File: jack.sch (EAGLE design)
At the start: 21 parts, among them IC1 NUF2221W1T2G, IC2 ATSAMD21G18, IC3 LDO, SW1 SPST

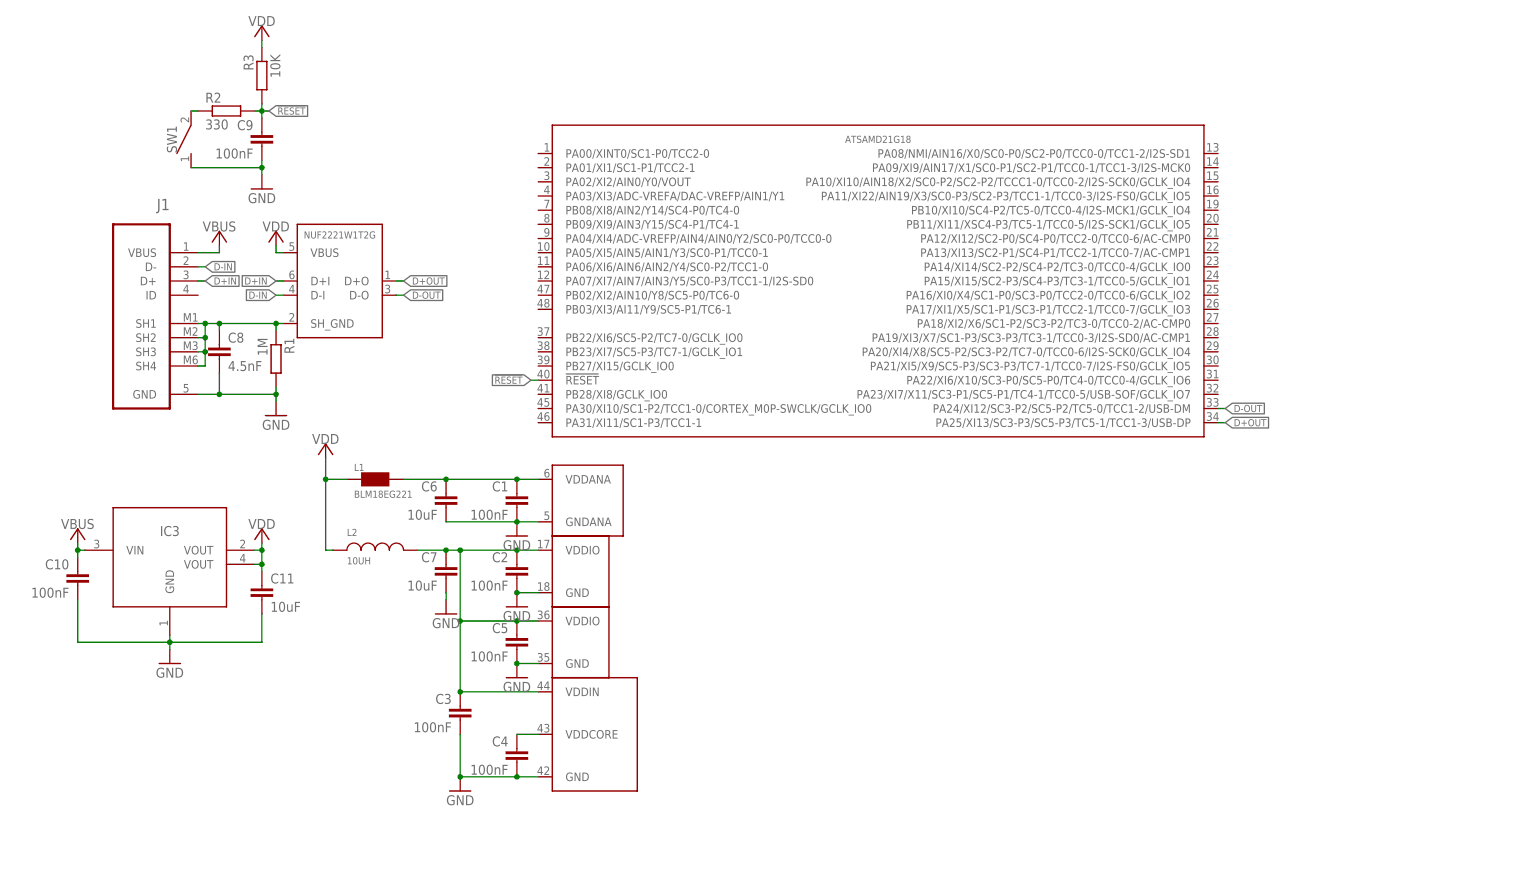
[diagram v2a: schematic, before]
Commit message: :goat: Added 24 MHZ crystal
Added 24 MHZ crystal
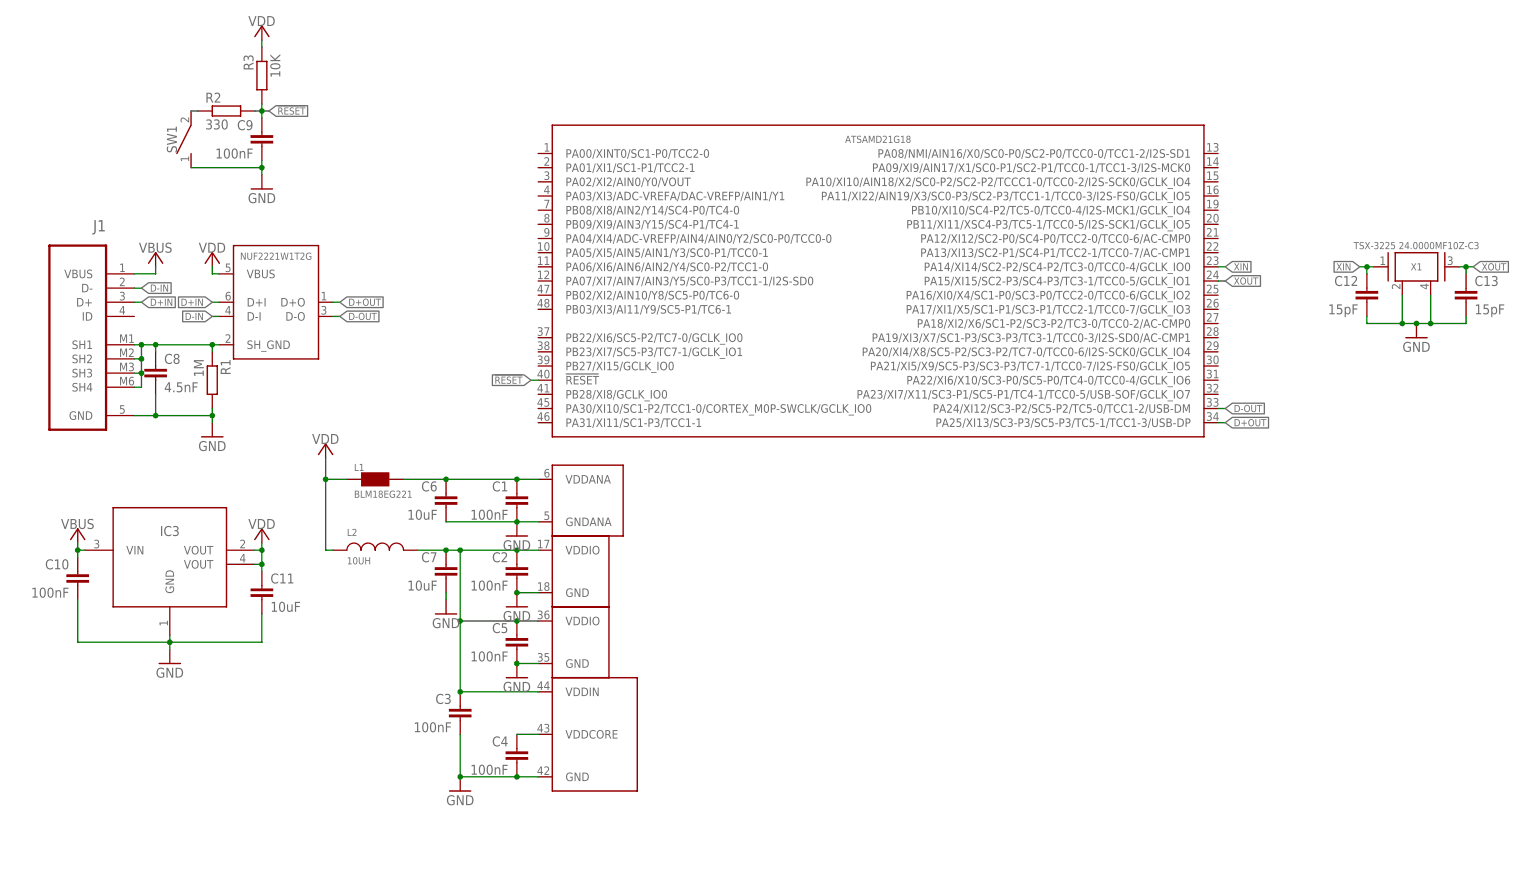
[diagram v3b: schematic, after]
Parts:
- added C12, C13: 15pF, rcl:C-EUC0603
- added X1: TSX-3225 24.0000MF10Z-C3, jack:XTAL
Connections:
- new net XIN: C12.1, IC2IO.PA14/XI14/SC2-P2/SC4-P2/TC3-0/TCC0-4/GCLK_IO0, X1.P$1
- new net XOUT: C13.1, IC2IO.PA15/XI15/SC2-P3/SC4-P3/TC3-1/TCC0-5/GCLK_IO1, X1.P$3
- net GND: now also C12.2, C13.2, X1.GND@1, X1.GND@2
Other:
- moved on the sheet: C8, J1, R1

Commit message: :memo: Added headers, protection diodes
Added protection diodes (reverse voltage/current for external power
input), dded pinout headers to schematic. Now I only got to decide how
to arrange pins on the breakout :smile:
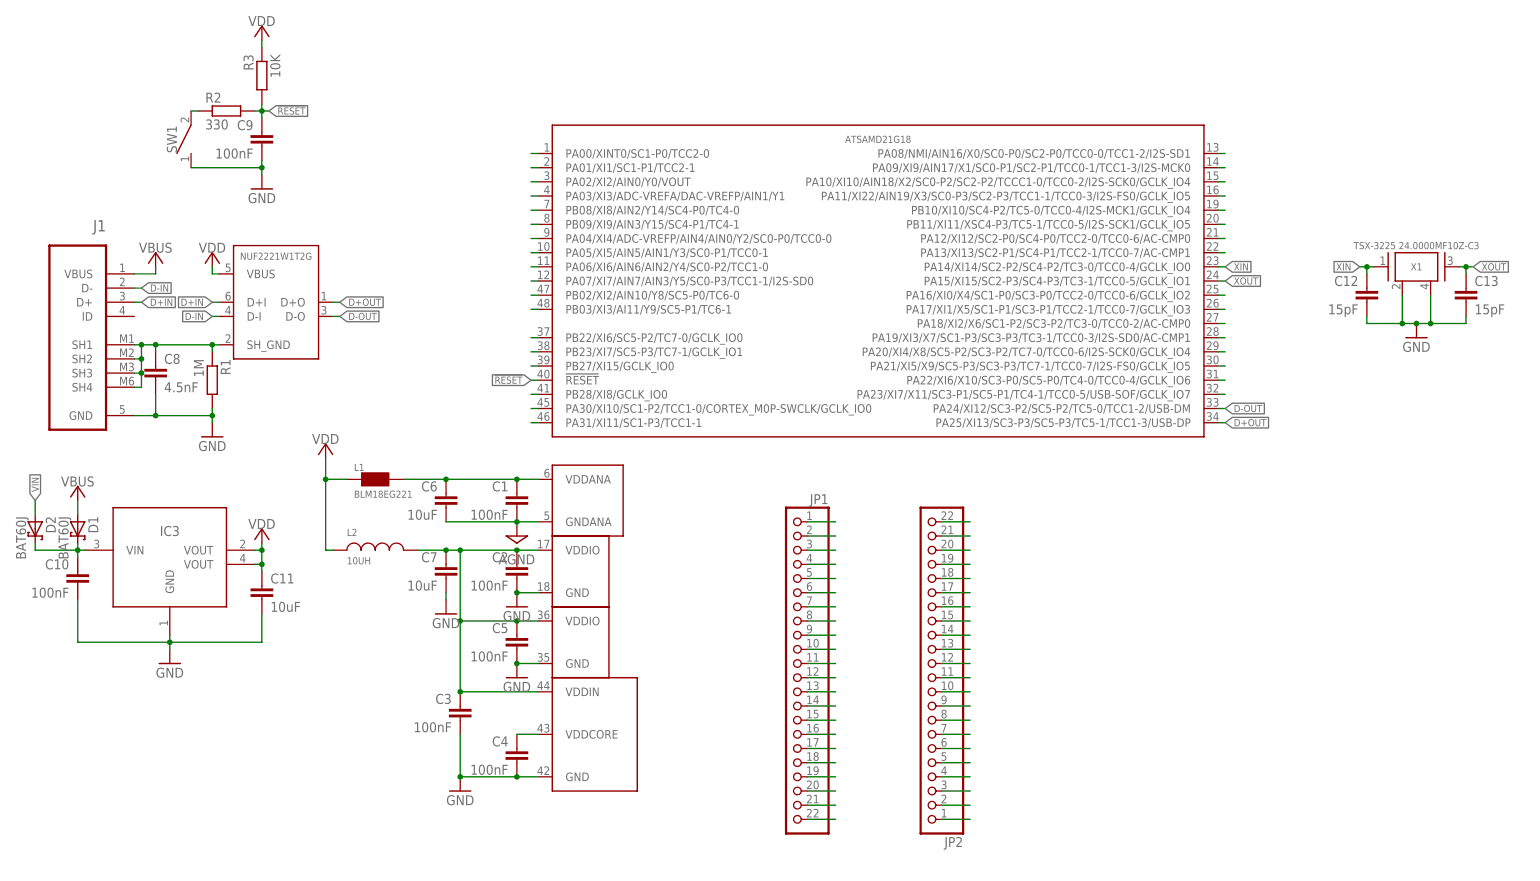
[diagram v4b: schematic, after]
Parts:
- added D1, D2: BAT60J, diode:BAT60J
- added JP1, JP2: (no value), pinhead:PINHD-1X22
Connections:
- net N$1 renamed VDDANA
- net N$4 renamed VDDIN
- new net 1: IC2IO.PA00/XINT0/SC1-P0/TCC2-0
- new net 10: IC2IO.PA05/XI5/AIN5/AIN1/Y3/SC0-P1/TCC0-1
- new net 11: IC2IO.PA06/XI6/AIN6/AIN2/Y4/SC0-P2/TCC1-0
- new net 12: IC2IO.PA07/XI7/AIN7/AIN3/Y5/SC0-P3/TCC1-1/I2S-SD0
- new net 13: IC2IO.PA08/NMI/AIN16/X0/SC0-P0/SC2-P0/TCC0-0/TCC1-2/I2S-SD1
- new net 14: IC2IO.PA09/XI9/AIN17/X1/SC0-P1/SC2-P1/TCC0-1/TCC1-3/I2S-MCK0
- new net 15: IC2IO.PA10/XI10/AIN18/X2/SC0-P2/SC2-P2/TCCC1-0/TCC0-2/I2S-SCK0/GCLK_IO4
- new net 16: IC2IO.PA11/XI22/AIN19/X3/SC0-P3/SC2-P3/TCC1-1/TCC0-3/I2S-FS0/GCLK_IO5
- new net 19: IC2IO.PB10/XI10/SC4-P2/TC5-0/TCC0-4/I2S-MCK1/GCLK_IO4
- new net 2: IC2IO.PA01/XI1/SC1-P1/TCC2-1
- new net 20: IC2IO.PB11/XI11/XSC4-P3/TC5-1/TCC0-5/I2S-SCK1/GCLK_IO5
- new net 21: IC2IO.PA12/XI12/SC2-P0/SC4-P0/TCC2-0/TCC0-6/AC-CMP0
- new net 22: IC2IO.PA13/XI13/SC2-P1/SC4-P1/TCC2-1/TCC0-7/AC-CMP1
- new net 25: IC2IO.PA16/XI0/X4/SC1-P0/SC3-P0/TCC2-0/TCC0-6/GCLK_IO2
- new net 26: IC2IO.PA17/XI1/X5/SC1-P1/SC3-P1/TCC2-1/TCC0-7/GCLK_IO3
- new net 27: IC2IO.PA18/XI2/X6/SC1-P2/SC3-P2/TC3-0/TCC0-2/AC-CMP0
- new net 28: IC2IO.PA19/XI3/X7/SC1-P3/SC3-P3/TC3-1/TCC0-3/I2S-SD0/AC-CMP1
- new net 29: IC2IO.PA20/XI4/X8/SC5-P2/SC3-P2/TC7-0/TCC0-6/I2S-SCK0/GCLK_IO4
- new net 3: IC2IO.PA02/XI2/AIN0/Y0/VOUT
- new net 30: IC2IO.PA21/XI5/X9/SC5-P3/SC3-P3/TC7-1/TCC0-7/I2S-FS0/GCLK_IO5
- new net 31: IC2IO.PA22/XI6/X10/SC3-P0/SC5-P0/TC4-0/TCC0-4/GCLK_IO6
- new net 32: IC2IO.PA23/XI7/X11/SC3-P1/SC5-P1/TC4-1/TCC0-5/USB-SOF/GCLK_IO7
- new net 37: IC2IO.PB22/XI6/SC5-P2/TC7-0/GCLK_IO0
- new net 38: IC2IO.PB23/XI7/SC5-P3/TC7-1/GCLK_IO1
- new net 39: IC2IO.PB27/XI15/GCLK_IO0
- new net 4: IC2IO.PA03/XI3/ADC-VREFA/DAC-VREFP/AIN1/Y1
- new net 41: IC2IO.PB28/XI8/GCLK_IO0
- new net 45: IC2IO.PA30/XI10/SC1-P2/TCC1-0/CORTEX_M0P-SWCLK/GCLK_IO0
- new net 46: IC2IO.PA31/XI11/SC1-P3/TCC1-1
- new net 47: IC2IO.PB02/XI2/AIN10/Y8/SC5-P0/TC6-0
- new net 48: IC2IO.PB03/XI3/AI11/Y9/SC5-P1/TC6-1
- new net 7: IC2IO.PB08/XI8/AIN2/Y14/SC4-P0/TC4-0
- new net 8: IC2IO.PB09/XI9/AIN3/Y15/SC4-P1/TC4-1
- new net 9: IC2IO.PA04/XI4/ADC-VREFP/AIN4/AIN0/Y2/SC0-P0/TCC0-0
- new net AGND: C1.2, C6.2, IC2PWR-ANA.GNDANA
- new net N$1: JP1.1
- new net N$10: JP1.8
- new net N$11: JP1.9
- new net N$12: JP1.10
- new net N$13: JP1.11
- new net N$14: JP1.12
- new net N$15: JP1.13
- new net N$16: JP1.14
- new net N$17: JP1.15
- new net N$18: JP1.16
- new net N$19: JP1.17
- new net N$2: C10.1, D1.C, D2.C, IC3.VIN
- new net N$20: JP1.18
- new net N$21: JP1.19
- new net N$22: JP1.20
- new net N$23: JP1.21
- new net N$24: JP1.22
- new net N$25: JP2.22
- new net N$26: JP2.21
- new net N$27: JP2.20
- new net N$28: JP2.19
- new net N$29: JP2.18
- new net N$30: JP2.17
- new net N$31: JP2.16
- new net N$32: JP2.15
- new net N$33: JP2.14
- new net N$34: JP2.13
- new net N$35: JP2.12
- new net N$36: JP2.11
- new net N$37: JP2.10
- new net N$38: JP2.9
- new net N$39: JP2.8
- new net N$4: JP1.2
- new net N$40: JP2.7
- new net N$41: JP2.6
- new net N$42: JP2.5
- new net N$43: JP2.4
- new net N$44: JP2.3
- new net N$45: JP2.2
- new net N$46: JP2.1
- new net N$5: JP1.3
- new net N$6: JP1.4
- new net N$7: JP1.5
- new net N$8: JP1.6
- new net N$9: JP1.7
- new net VIN: D2.A
- net GND: no longer C1.2, C6.2, IC2PWR-ANA.GNDANA
- net VBUS: now also D1.A; no longer C10.1, IC3.VIN

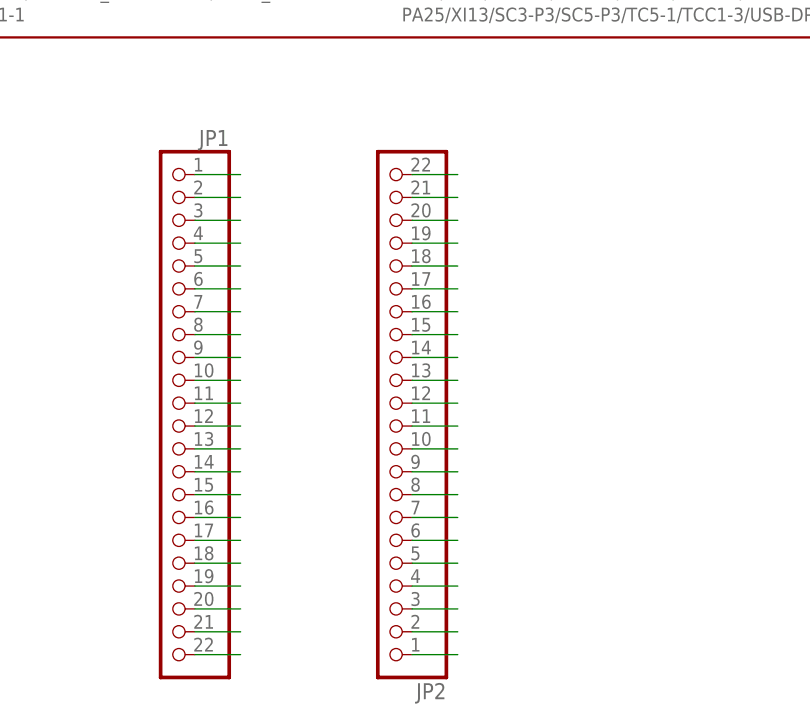
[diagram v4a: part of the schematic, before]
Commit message: :+1: Finished 1st schematic rev, created jack.brd
Finished first schematic revision (pin layout), created jack.brd layout
file, minor modifications to two downloaded component packages (text
size and position)
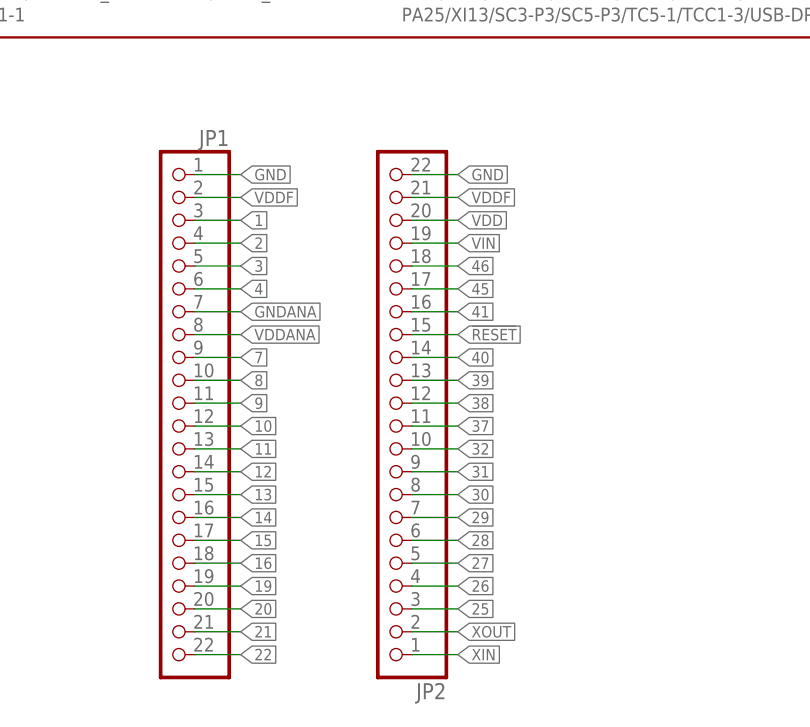
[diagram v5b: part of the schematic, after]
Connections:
- net N$33 renamed 40
- net N$9 renamed GNDANA
- removed net N$1: JP1.1
- removed net N$10: JP1.8
- removed net N$11: JP1.9
- removed net N$12: JP1.10
- removed net N$13: JP1.11
- removed net N$14: JP1.12
- removed net N$15: JP1.13
- removed net N$16: JP1.14
- removed net N$17: JP1.15
- removed net N$18: JP1.16
- removed net N$19: JP1.17
- removed net N$20: JP1.18
- removed net N$21: JP1.19
- removed net N$22: JP1.20
- removed net N$23: JP1.21
- removed net N$24: JP1.22
- removed net N$25: JP2.22
- removed net N$26: JP2.21
- removed net N$27: JP2.20
- removed net N$28: JP2.19
- removed net N$29: JP2.18
- removed net N$30: JP2.17
- removed net N$31: JP2.16
- removed net N$32: JP2.15
- removed net N$34: JP2.13
- removed net N$35: JP2.12
- removed net N$36: JP2.11
- removed net N$37: JP2.10
- removed net N$38: JP2.9
- removed net N$39: JP2.8
- removed net N$4: JP1.2
- removed net N$40: JP2.7
- removed net N$41: JP2.6
- removed net N$42: JP2.5
- removed net N$43: JP2.4
- removed net N$44: JP2.3
- removed net N$45: JP2.2
- removed net N$46: JP2.1
- removed net N$5: JP1.3
- removed net N$6: JP1.4
- removed net N$7: JP1.5
- removed net N$8: JP1.6
- removed net VDDIN: C2.1, C3.1, C5.1, C7.1, IC2PWR-IN-CORE.VDDIN, IC2PWR-IO1.VDDIO, IC2PWR-IO2.VDDIO, L2.1
- new net VDDF: C2.1, C3.1, C5.1, C7.1, IC2PWR-IN-CORE.VDDIN, IC2PWR-IO1.VDDIO, IC2PWR-IO2.VDDIO, JP1.2, JP2.21, L2.1
- net !RESET: now also JP2.15
- net 1: now also JP1.3
- net 10: now also JP1.12
- net 11: now also JP1.13
- net 12: now also JP1.14
- net 13: now also JP1.15
- net 14: now also JP1.16
- net 15: now also JP1.17
- net 16: now also JP1.18
- net 19: now also JP1.19
- net 2: now also JP1.4
- net 20: now also JP1.20
- net 21: now also JP1.21
- net 22: now also JP1.22
- net 25: now also JP2.3
- net 26: now also JP2.4
- net 27: now also JP2.5
- net 28: now also JP2.6
- net 29: now also JP2.7
- net 3: now also JP1.5
- net 30: now also JP2.8
- net 31: now also JP2.9
- net 32: now also JP2.10
- net 37: now also JP2.11
- net 38: now also JP2.12
- net 39: now also JP2.13
- net 4: now also JP1.6
- net 41: now also JP2.16
- net 45: now also JP2.17
- net 46: now also JP2.18
- net 7: now also JP1.9
- net 8: now also JP1.10
- net 9: now also JP1.11
- net GND: now also JP1.1, JP2.22
- net VDD: now also JP2.20
- net VDDANA: now also JP1.8
- net VIN: now also JP2.19
- net XIN: now also JP2.1
- net XOUT: now also JP2.2
